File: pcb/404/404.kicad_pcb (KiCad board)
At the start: 2 copper layers, 52 x 63 mm, 43 parts, among them J1 Conn_01x04, Q1 BC846, U1 RC4558

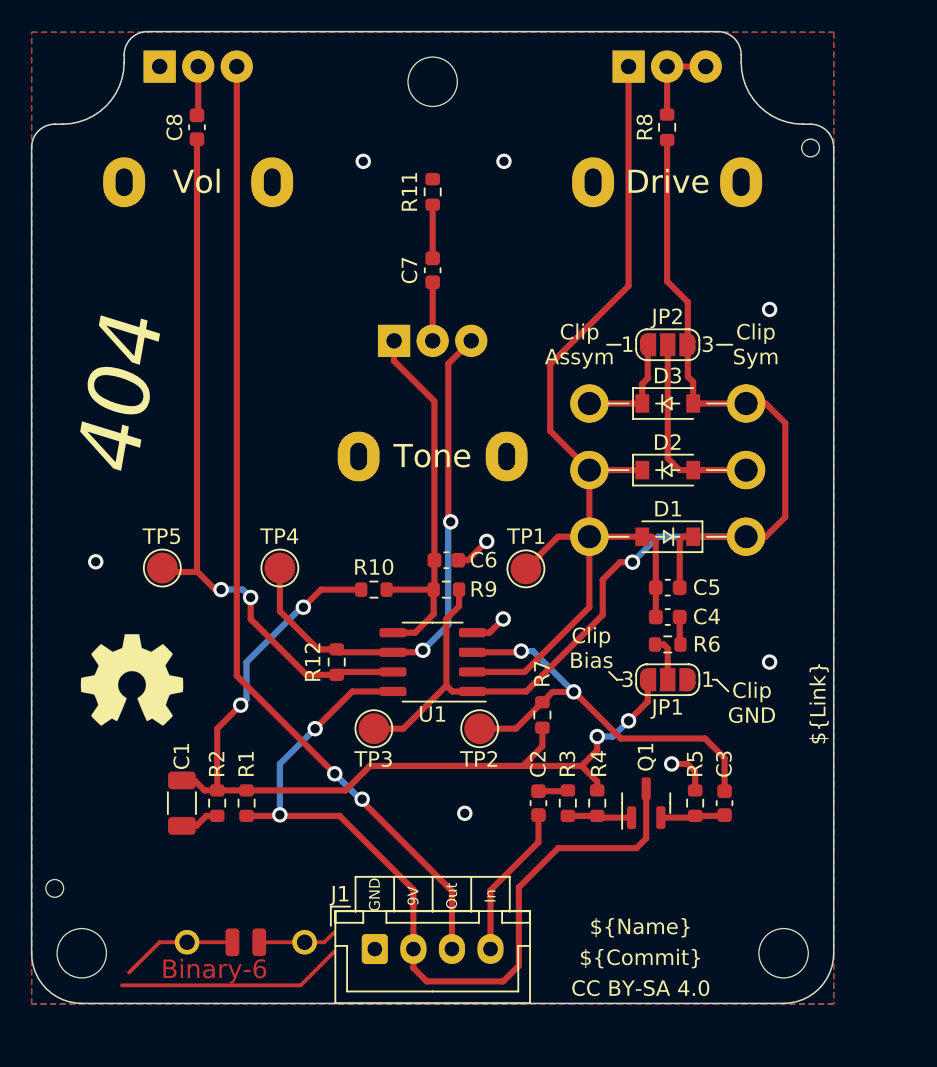
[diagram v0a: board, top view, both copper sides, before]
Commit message: [404] Recreate Upper and Front PCBs according to new base templates
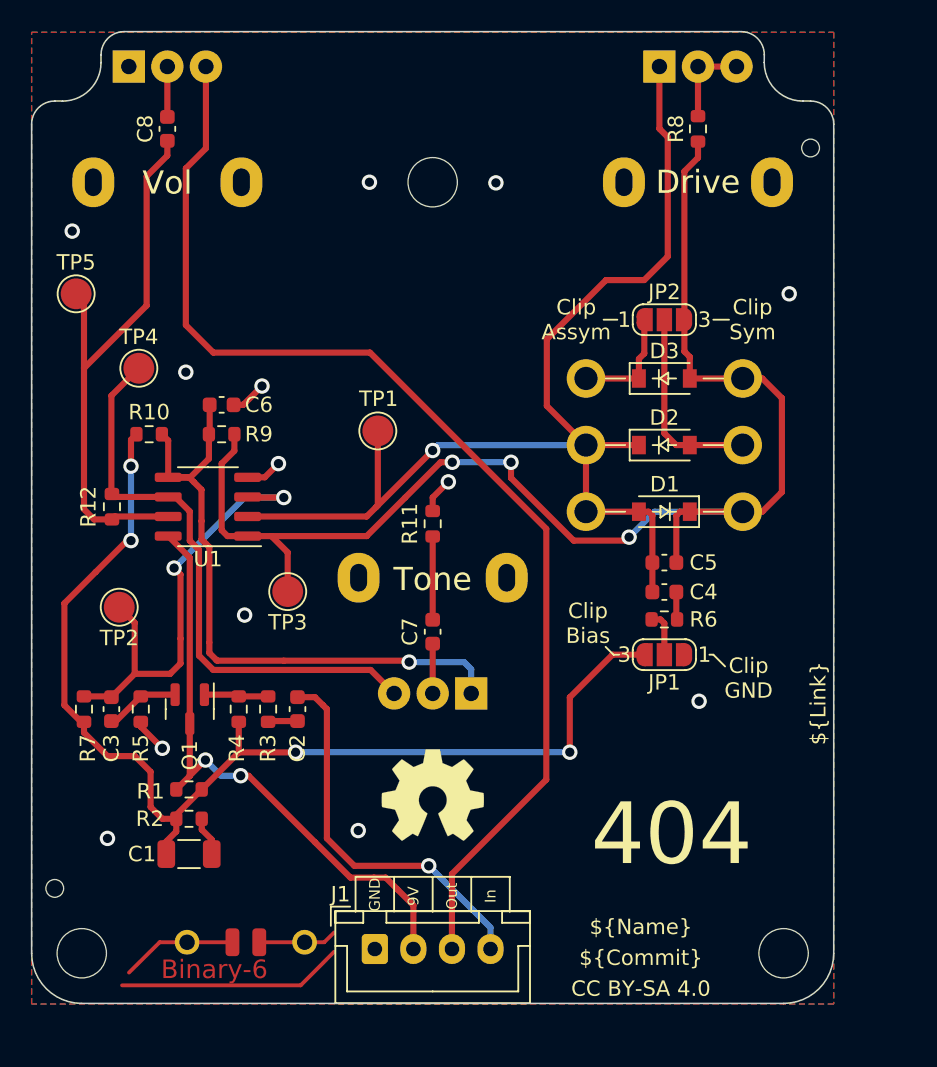
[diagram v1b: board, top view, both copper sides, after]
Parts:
- moved C3 40.2 mm to (128.7, 111.4)
- moved R5 36.5 mm to (130.6, 111.4), turned to -90 degrees
- moved Q1 30.2 mm to (133.8, 111.4), turned to -90 degrees
- moved R7 29.7 mm to (126.9, 111.4)
- moved TP2 24.7 mm to (129.2, 104.8)
- moved R4 24.0 mm to (136.9, 111.4), turned to 90 degrees
- moved C7 23.4 mm to (149.5, 106.4)
- moved RV2 23.4 mm to (152.0, 110.4), turned to 90 degrees
- moved R11 21.5 mm to (149.5, 99.4)
- moved REF** 20.9 mm to (149.5, 117.0)
- moved R3 20.4 mm to (138.8, 111.4), turned to 90 degrees
- moved TP5 18.6 mm to (126.4, 84.5)
- moved C6 17.7 mm to (135.8, 91.7)
- moved R9 17.7 mm to (135.8, 93.6)
- moved R10 17.7 mm to (131.1, 93.6)
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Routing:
- net +9V: track 55.9 -> 39.0 mm
- net Net-(C6-Pad1): track 25.0 -> 41.9 mm, vias 0 -> 1
- net Upper_PCB_Input: track 9.97 -> 25.0 mm, vias 0 -> 1
- net +4V5: track 58.3 -> 73.2 mm
- net Upper_PCB_Output: track 63.1 -> 75.9 mm, vias 2 -> 0
- net Net-(C4-Pad1): track 65.3 -> 76.5 mm, vias 0 -> 1
- net Net-(C5-Pad2): track 78.4 -> 89.0 mm, vias 1 -> 3
- net Net-(C8-Pad1): track 46.8 -> 37.0 mm, vias 2 -> 0
- net Net-(R12-Pad1): track 34.7 -> 37.7 mm, vias 2 -> 0
- net Net-(C7-Pad2): track 3.48 -> 5.40 mm
- net GND: track 10.2 -> 11.9 mm, vias 9 -> 6
- net Net-(C3-Pad2): track 28.5 -> 29.6 mm
- net Net-(C3-Pad1): track 4.20 -> 4.84 mm
- net Net-(C7-Pad1): track 3.80 -> 3.22 mm
- net (no net): vias 0 -> 7
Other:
- outline, holes or cut-outs redrawn

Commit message: [404] Minor design improvements
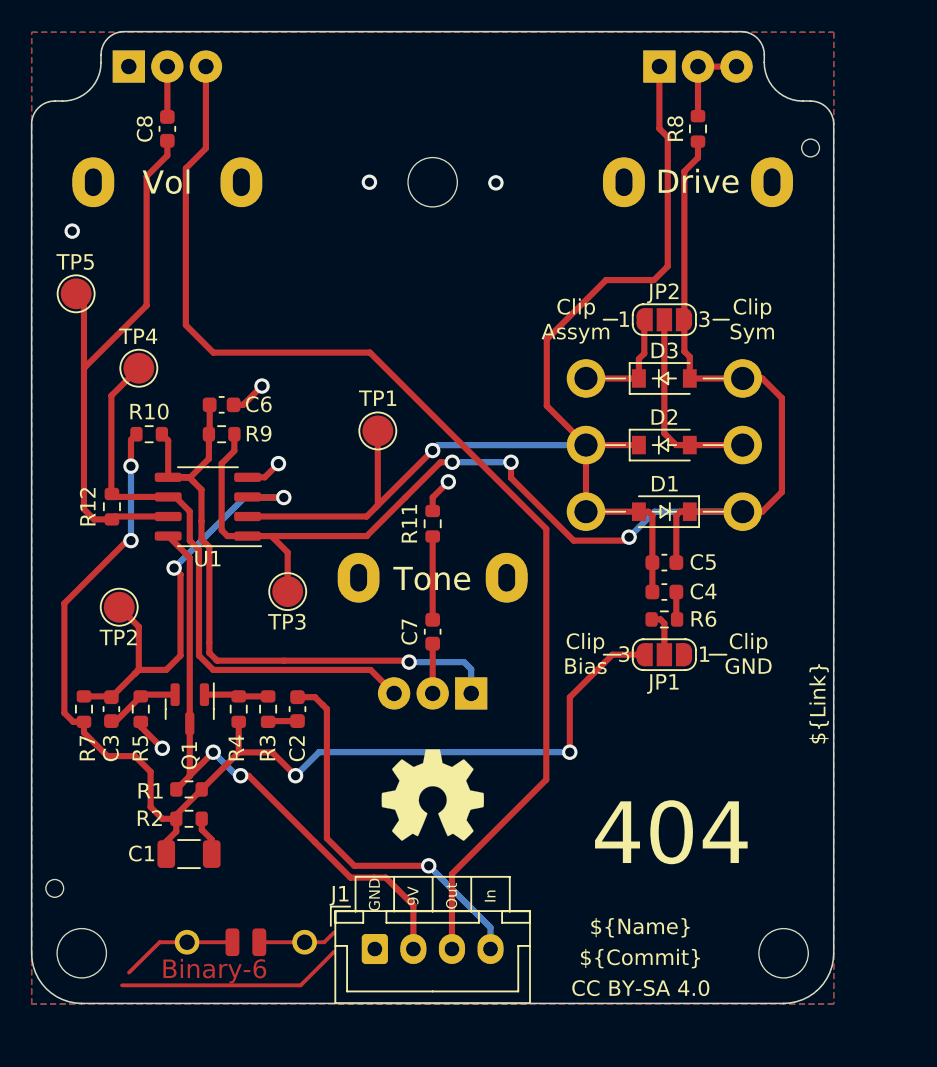
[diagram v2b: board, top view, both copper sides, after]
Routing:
- net +4V5: track 73.2 -> 74.8 mm
- net (no net): vias 7 -> 1

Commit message: [All] Flip board to board connector on upper PCB (obstructed some silk)
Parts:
- moved J1 7.57 mm to (153.2, 128.0), turned to 180 degrees
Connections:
- J1 pad 1: GND -> Upper_PCB_Input
- J1 pad 2: +9V -> Upper_PCB_Output
- J1 pad 3: Upper_PCB_Output -> +9V
- J1 pad 4: Upper_PCB_Input -> GND
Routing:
- net Upper_PCB_Output: track 75.9 -> 77.0 mm
- net Upper_PCB_Input: track 25.0 -> 26.1 mm
- net +9V: track 39.5 -> 40.5 mm

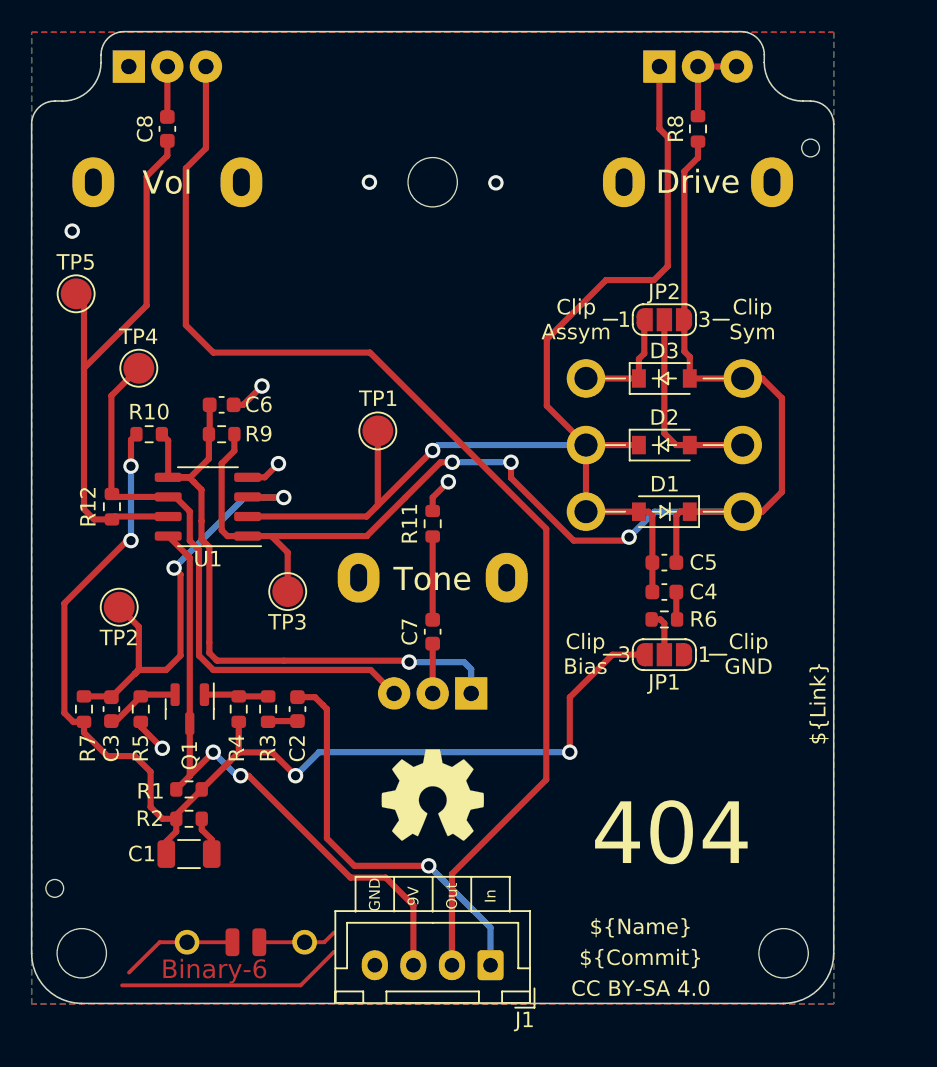
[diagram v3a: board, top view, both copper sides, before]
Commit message: [404][UpperRaw] Apply learned lessons from TOP:
- Name on silk etc. is now a text variable
- Optimized copypasta parts
- Set pot footprint to my modified one
- Rename pots ro always be RV1-6
- Use text variables for pot names
- Show pot values on silk
- Update board constraints to JLCPCB capabilities
- Add Gndpour to UpperRaw
- Set "Not in schematic" for OSHW logo
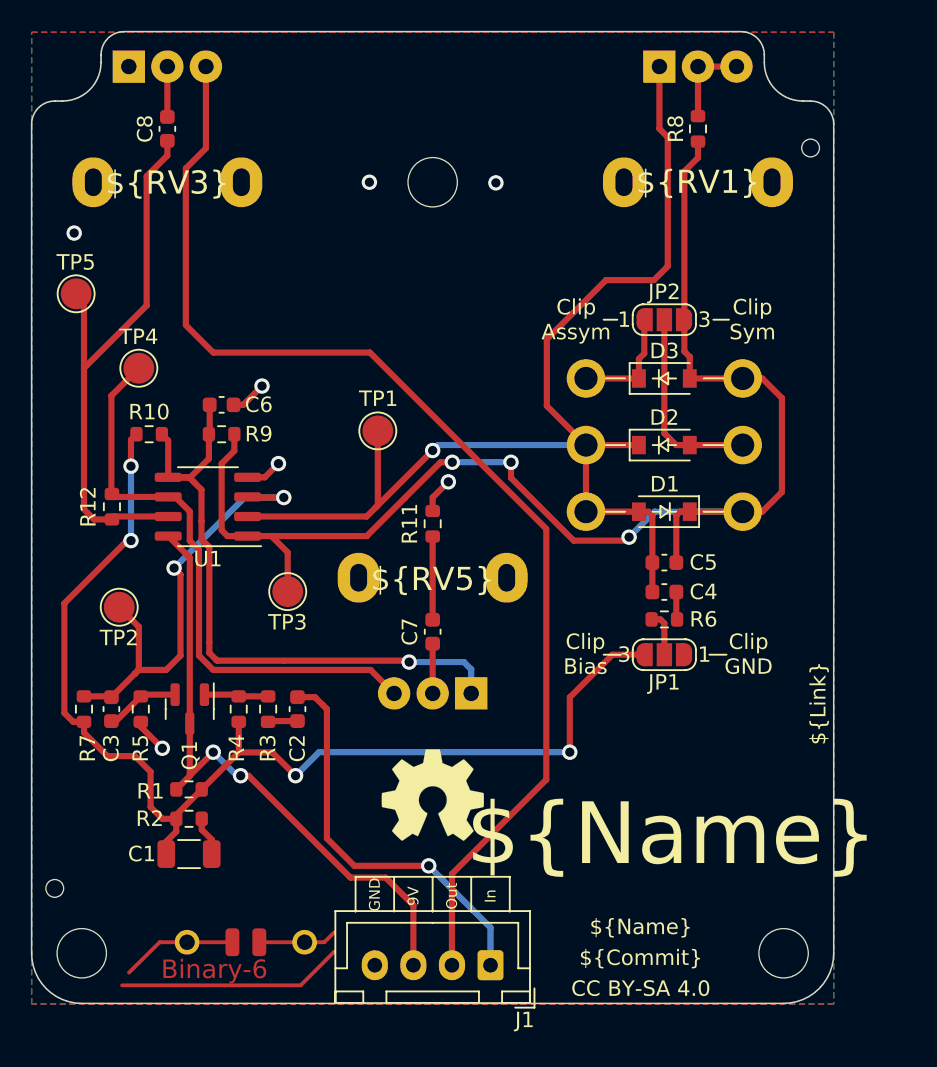
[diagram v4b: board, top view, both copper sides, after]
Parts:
- RV1: value 500K -> 500K Log
- RV3: value 100K -> 100K Lin
- RV5: renamed from RV2; value 20k -> 20k W
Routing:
- net GND: vias 6 -> 7
- net (no net): vias 1 -> 0
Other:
- board text added: "${RV1}"
- board text added: "${RV3}"
- board text added: "${RV5}"
- board text removed: "404"
- board text removed: "Drive"
- board text removed: "Tone"
- board text removed: "Vol"
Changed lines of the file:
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@@
     (solder_mask_min_width 0.254)
     (aux_axis_origin 149.5 67.5)
-    (grid_origin 149.5 110.405)
+    (grid_origin 149.5 67.5)
     (pcbplotparams
       (layerselection 0x00010fc_ffffffff)
@@
   (property "Link" "gitlab.com/Chrismettal/pedaldev")
   (property "Name" "404")
+  (property "RV1" "Drive")
+  (property "RV3" "Vol")
+  (property "RV5" "Tone")
   (net 0 "")
   (net 1 "+9V")
@@
     (descr "Open Source Hardware Symbol")
     (tags "Logo Symbol OSHW")
-    (attr exclude_from_pos_files exclude_from_bom)
+    (attr board_only exclude_from_pos_files exclude_from_bom)
     (fp_text reference "REF**" (at 0 0) (layer "F.SilkS") hide
       (effects (font (size 1 1) (thickness 0.15)))
@@
     (property "Sheetname" "")
     (attr through_hole)
-    (fp_text reference "RV1" (at 11.176 -8.2296 90) (layer "B.SilkS")
+    (fp_text reference "RV1" (at 3.429 3.143 90) (layer "B.SilkS")
       (effects (font (size 1 1) (thickness 0.15)) (justify mirror))
     )
-    (fp_text value "500K" (at 2.54 -2.5 180) (layer "B.Fab")
+    (fp_text value "500K Log" (at 10.287 -9.938 -90) (layer "B.SilkS")
       (effects (font (size 1 1) (thickness 0.15)) (justify mirror))
     )
@@
     (property "Sheetname" "")
     (attr through_hole)
-    (fp_text reference "RV3" (at 11.1252 -8.2804 90) (layer "B.SilkS")
+    (fp_text reference "RV3" (at 3.937 3.033 90) (layer "B.SilkS")
       (effects (font (size 1 1) (thickness 0.15)) (justify mirror))
     )
-    (fp_text value "100K" (at 2.54 -2.5) (layer "B.Fab")
+    (fp_text value "100K Lin" (at 2.286 -8.143 90) (layer "B.SilkS")
       (effects (font (size 1 1) (thickness 0.15)) (justify mirror))
     )
@@
     (property "Sheetname" "")
     (attr through_hole)
-    (fp_text reference "RV2" (at 11.176 -8.2404 90) (layer "B.SilkS")
+    (fp_text reference "RV5" (at 3.683 -8.088 90) (layer "B.SilkS")
       (effects (font (size 1 1) (thickness 0.15)) (justify mirror))
     )
-    (fp_text value "20k" (at 2.54 -2.5) (layer "B.Fab")
+    (fp_text value "20k W" (at 2.54 3.088 90) (layer "B.SilkS")
       (effects (font (size 1 1) (thickness 0.15)) (justify mirror))
     )
@@
   (gr_line (start 167.441 107.893) (end 168.55 107.893) (layer "F.SilkS") (width 0.12))
   (gr_line (start 149.5 67.545) (end 149.5 130.545) (layer "Eco1.User") (width 0.15))
-  (gr_line (start 175.5 73.5) (end 175.5 127.25) (layer "Edge.Cuts") (width 0.1))
-  (gr_arc (start 173.5 72.005) (mid 171.73047 71.273073) (end 170.995005 69.50501) (layer "Edge.Cuts") (width 0.1))
-  (gr_arc (start 126.75 130.5) (mid 124.451903 129.548097) (end 123.5 127.25) (layer "Edge.Cuts") (width 0.1))
   (gr_line (start 123.5 73.5) (end 123.5 127.25) (layer "Edge.Cuts") (width 0.1))
-  (gr_arc (start 123.5 73.5) (mid 123.93934 72.43934) (end 125 72) (layer "Edge.Cuts") (width 0.1))
-  (gr_line (start 170.995005 69.50501) (end 171 69) (layer "Edge.Cuts") (width 0.1))
-  (gr_line (start 126.75 130.5) (end 172.25 130.5) (layer "Edge.Cuts") (width 0.1))
-  (gr_line (start 128 69) (end 128 69.505) (layer "Edge.Cuts") (width 0.1))
-  (gr_arc (start 128 69.505) (mid 127.267767 71.272767) (end 125.5 72.005) (layer "Edge.Cuts") (width 0.1))
-  (gr_arc (start 175.5 127.25) (mid 174.548097 129.548097) (end 172.25 130.5) (layer "Edge.Cuts") (width 0.1))
-  (gr_line (start 173.5 72) (end 174 72) (layer "Edge.Cuts") (width 0.1))
-  (gr_arc (start 128 69) (mid 128.43934 67.93934) (end 129.5 67.5) (layer "Edge.Cuts") (width 0.1))
-  (gr_arc (start 169.5 67.5) (mid 170.56066 67.93934) (end 171 69) (layer "Edge.Cuts") (width 0.1))
-  (gr_line (start 125 72) (end 125.5 72) (layer "Edge.Cuts") (width 0.1))
   (gr_line (start 129.5 67.5) (end 169.5 67.5) (layer "Edge.Cuts") (width 0.1))
   (gr_arc (start 174 72) (mid 175.06066 72.43934) (end 175.5 73.5) (layer "Edge.Cuts") (width 0.1))
-  (gr_text "Tone" (at 149.5 113.005) (layer "B.SilkS")
+  (gr_arc (start 128 69.5) (mid 127.267767 71.267767) (end 125.5 72) (layer "Edge.Cuts") (width 0.1))
+  (gr_arc (start 126.75 130.5) (mid 124.451903 129.548097) (end 123.5 127.25) (layer "Edge.Cuts") (width 0.1))
+  (gr_line (start 126.75 130.5) (end 172.25 130.5) (layer "Edge.Cuts") (width 0.1))
+  (gr_line (start 173.5 72) (end 174 72) (layer "Edge.Cuts") (width 0.1))
+  (gr_line (start 125 72) (end 125.5 72) (layer "Edge.Cuts") (width 0.1))
+  (gr_arc (start 175.5 127.25) (mid 174.548097 129.548097) (end 172.25 130.5) (layer "Edge.Cuts") (width 0.1))
+  (gr_arc (start 173.5 72) (mid 171.732233 71.267767) (end 171 69.5) (layer "Edge.Cuts") (width 0.1))
+  (gr_arc (start 169.5 67.5) (mid 170.56066 67.93934) (end 171 69) (layer "Edge.Cuts") (width 0.1))
+  (gr_arc (start 128 69) (mid 128.43934 67.93934) (end 129.5 67.5) (layer "Edge.Cuts") (width 0.1))
+  (gr_arc (start 123.5 73.5) (mid 123.93934 72.43934) (end 125 72) (layer "Edge.Cuts") (width 0.1))
+  (gr_line (start 175.5 73.5) (end 175.5 127.25) (layer "Edge.Cuts") (width 0.1))
+  (gr_line (start 171 69.5) (end 171 69) (layer "Edge.Cuts") (width 0.1))
+  (gr_line (start 128 69.5) (end 128 69) (layer "Edge.Cuts") (width 0.1))
+  (gr_text "${RV5}" (at 149.5 113.005) (layer "B.SilkS")
     (effects (font (size 1.5 1.5) (thickness 0.3)) (justify mirror))
   )
@@
     (effects (font (size 1 1) (thickness 0.2)) (justify mirror))
   )
-  (gr_text "Drive" (at 166.7 83.405) (layer "B.SilkS")
+  (gr_text "${RV1}" (at 166.7 83.405) (layer "B.SilkS")
     (effects (font (size 1.5 1.5) (thickness 0.3)) (justify mirror))
   )
-  (gr_text "Vol" (at 132.3 83.505) (layer "B.SilkS")
+  (gr_text "${RV3}" (at 132.3 83.505) (layer "B.SilkS")
     (effects (font (size 1.5 1.5) (thickness 0.3)) (justify mirror))
   )
-  (gr_text "404" (at 164.994 119.549) (layer "F.SilkS")
+  (gr_text "${Name}" (at 164.994 119.549) (layer "F.SilkS")
     (effects (font (size 4 4) (thickness 1)))
   )
-  (gr_text "Tone" (at 149.5 103.005) (layer "F.SilkS")
+  (gr_text "${RV5}" (at 149.5 103.005) (layer "F.SilkS")
     (effects (font (size 1.5 1.5) (thickness 0.3)))
   )
@@
     (effects (font (size 1 1) (thickness 0.15)))
   )
-  (gr_text "Vol" (at 132.3 77.305) (layer "F.SilkS")
+  (gr_text "${RV3}" (at 132.3 77.305) (layer "F.SilkS")
     (effects (font (size 1.5 1.5) (thickness 0.3)))
   )
@@
     (effects (font (size 1 1) (thickness 0.15)))
   )
-  (gr_text "Drive" (at 166.7 77.258) (layer "F.SilkS")
+  (gr_text "${RV1}" (at 166.7 77.258) (layer "F.SilkS")
     (effects (font (size 1.5 1.5) (thickness 0.3)))
   )
@@
     (effects (font (size 0.7 0.7) (thickness 0.13)))
   )
-  (gr_text "404" (at 164.994 119.549) (layer "F.Mask")
+  (gr_text "${Name}" (at 164.994 119.549) (layer "F.Mask")
     (effects (font (size 4 4) (thickness 0.6)))
   )
-  (via (at 126.132 80.433) (size 1) (drill 0.6) (layers "F.Cu" "B.Cu") (net 0))
   (segment (start 133.752 115.739) (end 133.752 115.754) (width 0.4) (layer "F.Cu") (net 1))
   (segment (start 132.878 116.628) (end 133.752 115.754) (width 0.4) (layer "F.Cu") (net 1))
@@
   (via (at 139.502 95.506) (size 1) (drill 0.6) (layers "F.Cu" "B.Cu") (net 2))
   (via (at 131.974 113.961) (size 1) (drill 0.6) (layers "F.Cu" "B.Cu") (net 2))
+  (via (at 126.259 80.56) (size 1) (drill 0.6) (layers "F.Cu" "B.Cu") (free) (net 2))
   (via (at 145.4 77.265) (size 1) (drill 0.6) (layers "F.Cu" "B.Cu") (free) (net 2))
   (via (at 150.516 96.689) (size 1) (drill 0.6) (layers "F.Cu" "B.Cu") (net 2))
